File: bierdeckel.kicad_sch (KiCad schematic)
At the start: 15 parts, among them J1 S70-332002045R, J2 S70-332002045R, J3 S70-332002045R, J4 S70-332002045R, SW1 Address Coding, SW2 PTS526 SK15 SMTR2 LFS, SW3 PTS526 SK15 SMTR2 LFS, U1 ESP32-C3-WROOM-02

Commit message: change to 2 pressure gauge strips
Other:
- moved on the sheet: B5
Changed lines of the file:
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@@
 	(symbol
 		(lib_id "power:GND")
-		(at 77.47 86.36 0)
-		(unit 1)
-		(exclude_from_sim no)
-		(in_bom yes)
-		(on_board yes)
-		(dnp no)
-		(fields_autoplaced yes)
+		(at 45.72 78.74 0)
+		(unit 1)
+		(exclude_from_sim no)
+		(in_bom yes)
+		(on_board yes)
+		(dnp no)
 		(property "Reference" "#PWR013"
-			(at 77.47 92.71 0)
+			(at 45.72 85.09 0)
 			(effects
 				(font
@@
 		)
 		(property "Value" "GND"
-			(at 77.47 91.44 0)
+			(at 45.72 82.804 0)
 			(effects
 				(font
@@
 		)
 		(property "Footprint" ""
-			(at 77.47 86.36 0)
+			(at 45.72 78.74 0)
 			(effects
 				(font
@@
 		)
 		(property "Datasheet" ""
-			(at 77.47 86.36 0)
+			(at 45.72 78.74 0)
 			(effects
 				(font
@@
 		)
 		(property "Description" "Power symbol creates a global label with name \"GND\" , ground"
-			(at 77.47 86.36 0)
+			(at 45.72 78.74 0)
 			(effects
 				(font
@@
 	(symbol
 		(lib_id "power:GND")
-		(at 77.47 78.74 180)
-		(unit 1)
-		(exclude_from_sim no)
-		(in_bom yes)
-		(on_board yes)
-		(dnp no)
-		(fields_autoplaced yes)
+		(at 45.72 71.12 180)
+		(unit 1)
+		(exclude_from_sim no)
+		(in_bom yes)
+		(on_board yes)
+		(dnp no)
 		(property "Reference" "#PWR012"
-			(at 77.47 72.39 0)
+			(at 45.72 64.77 0)
 			(effects
 				(font
@@
 		)
 		(property "Value" "GND"
-			(at 77.47 73.66 0)
+			(at 45.72 67.31 0)
 			(effects
 				(font
@@
 		)
 		(property "Footprint" ""
-			(at 77.47 78.74 0)
+			(at 45.72 71.12 0)
 			(effects
 				(font
@@
 		)
 		(property "Datasheet" ""
-			(at 77.47 78.74 0)
+			(at 45.72 71.12 0)
 			(effects
 				(font
@@
 		)
 		(property "Description" "Power symbol creates a global label with name \"GND\" , ground"
-			(at 77.47 78.74 0)
+			(at 45.72 71.12 0)
 			(effects
 				(font
@@
 	(symbol
 		(lib_id "Device:R")
-		(at 77.47 82.55 0)
+		(at 45.72 74.93 0)
 		(unit 1)
 		(exclude_from_sim no)
@@
 		(fields_autoplaced yes)
 		(property "Reference" "B5"
-			(at 80.01 81.28 0)
+			(at 48.26 73.66 0)
 			(effects
 				(font
@@
 		)
 		(property "Value" "0R"
-			(at 80.01 83.82 0)
+			(at 48.26 76.2 0)
 			(effects
 				(font
@@
 		)
 		(property "Footprint" "Resistor_SMD:R_1206_3216Metric"
-			(at 75.692 82.55 90)
+			(at 43.942 74.93 90)
 			(effects
 				(font
@@
 		)
 		(property "Datasheet" "~"
-			(at 77.47 82.55 0)
+			(at 45.72 74.93 0)
 			(effects
 				(font
@@
 		)
 		(property "Description" "Resistor"
-			(at 77.47 82.55 0)
+			(at 45.72 74.93 0)
 			(effects
 				(font
@@
 		)
 		(property "mpn" "CR1206-J/-000ELF"
-			(at 77.47 82.55 0)
-			(effects
-				(font
+			(at 45.72 74.93 0)
+			(effects
+				(font

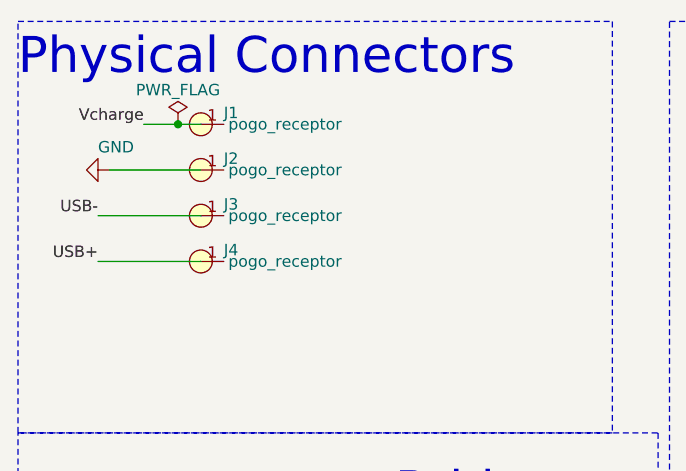
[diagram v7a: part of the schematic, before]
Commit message: update design; add 3d models to everything; add notches to PCB
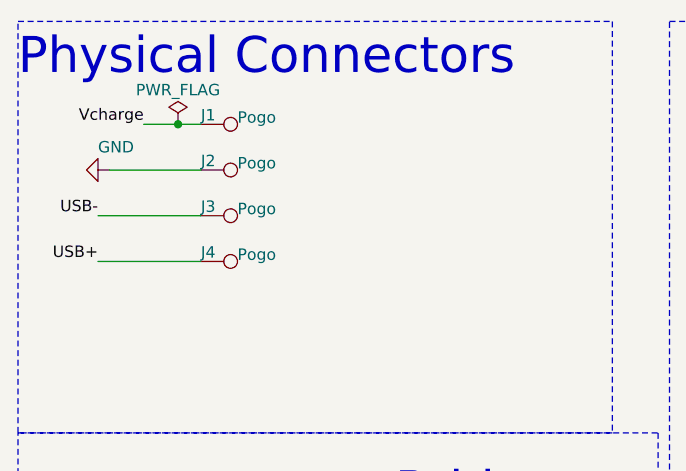
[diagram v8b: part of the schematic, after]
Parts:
- removed J1, J2, J3, J4: S70-332002045R, bier:pogo_receptor, symbol bier:Pogo_receptor
- added J1, J2, J3, J4: Pogo, TestPoint:TestPoint_Pad_D3.0mm, symbol Connector:TestPoint
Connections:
- net GND: now also J2.1
- net USB+: now also J4.1
- net USB-: now also J3.1
- net Vcharge: now also J1.1
